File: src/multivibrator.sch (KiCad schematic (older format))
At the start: 11 parts, among them CON1 BARREL_JACK, Q1 Q_NPN_EBC, Q2 Q_NPN_EBC

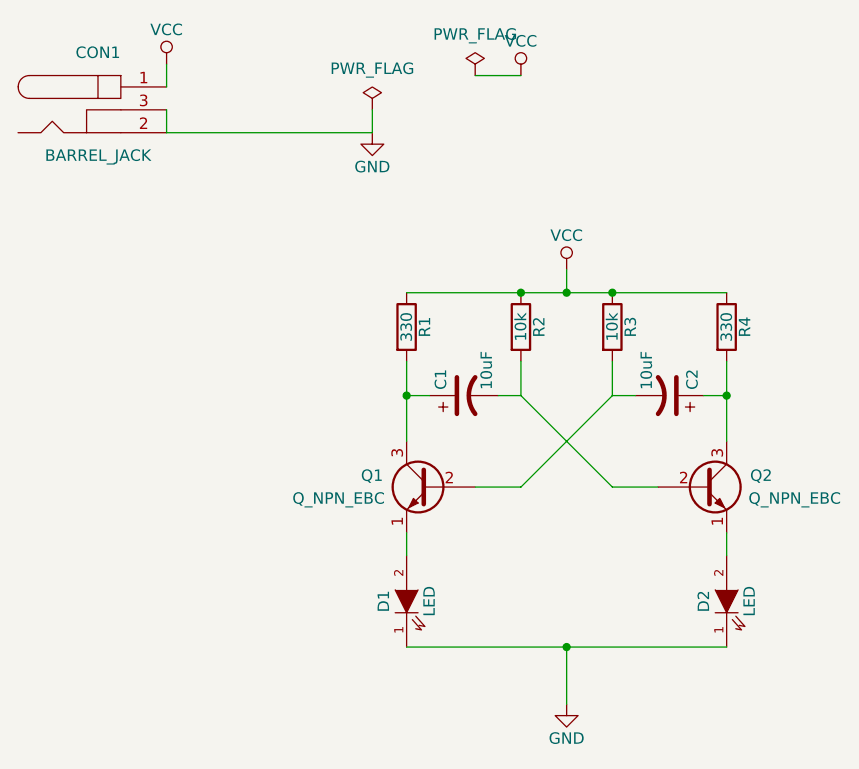
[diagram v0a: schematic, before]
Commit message: use smaller connector
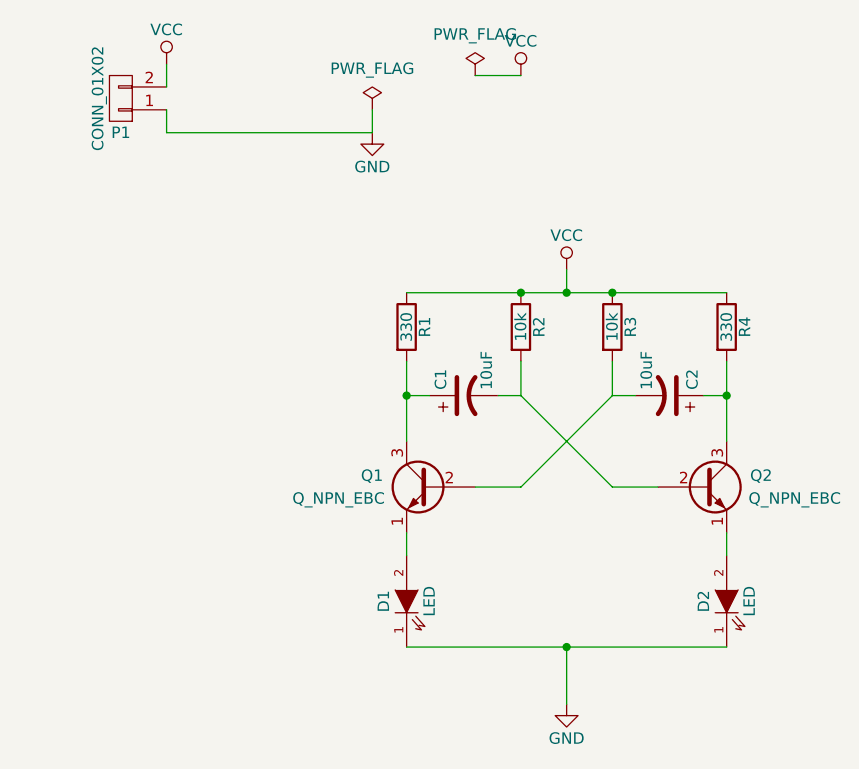
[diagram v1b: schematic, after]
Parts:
- removed CON1: BARREL_JACK, Connect:BARREL_JACK, symbol BARREL_JACK
- added P1: CONN_01X02, Socket_Strips:Socket_Strip_Straight_1x02_Pitch2.54mm, symbol CONN_01X02
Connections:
- net GND: now also P1.1 (P1)
- net VCC: now also P1.2 (P2)
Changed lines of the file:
@@
 $EndComp
 Wire Wire Line
-	3350 2100 3350 2200
+	3350 2200 3350 2100
 Wire Wire Line
 	2650 2200 4050 2200
@@
 Wire Wire Line
 	2500 1400 2500 1500
-$Comp
-L BARREL_JACK CON1
-U 1 1 57D02787
-P 1300 1400
-F 0 "CON1" H 1300 1650 50  0000 C CNN
-F 1 "BARREL_JACK" H 1300 1200 50  0000 C CNN
-F 2 "Connect:BARREL_JACK" H 1300 1400 50  0001 C CNN
-F 3 "" H 1300 1400 50  0000 C CNN
-	1    1300 1400
-	1    0    0    -1
-$EndComp
 Wire Wire Line
 	2500 1500 1600 1500
@@
 	1    0    0    -1
 $EndComp
+$Comp
+L CONN_01X02 P1
+U 1 1 591D84EF
+P 1400 1350
+F 0 "P1" H 1400 1500 50  0000 C CNN
+F 1 "CONN_01X02" V 1500 1350 50  0000 C CNN
+F 2 "Socket_Strips:Socket_Strip_Straight_1x02_Pitch2.54mm" H 1400 1350 50  0001 C CNN
+F 3 "" H 1400 1350 50  0000 C CNN
+	1    1400 1350
+	-1   0    0    1
+$EndComp
 $EndSCHEMATC

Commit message: update kicad, rotate connector, clean up trace
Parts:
- D1, D2: symbol LED -> LED-RESCUE-multivibrator
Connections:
- net GND: now also P1.2 (P2); no longer P1.1 (P1)
- net VCC: now also P1.1 (P1); no longer P1.2 (P2)
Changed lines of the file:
@@
 EESchema Schematic File Version 2
+LIBS:multivibrator-rescue
 LIBS:power
 LIBS:device
@@
 $EndComp
 $Comp
-L LED D2
+L LED-RESCUE-multivibrator D2
 U 1 1 57D0105D
 P 4050 3550
@@
 $EndComp
 $Comp
-L LED D1
+L LED-RESCUE-multivibrator D1
 U 1 1 57D0111A
 P 2650 3550
@@
 F 3 "" H 1400 1350 50  0000 C CNN
 	1    1400 1350
-	-1   0    0    1
+	-1   0    0    -1
 $EndComp
 $EndSCHEMATC
